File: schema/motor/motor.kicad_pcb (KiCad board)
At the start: 2 copper layers, 50 x 50 mm, 13 parts, among them IC1 RP2040_ZERO, J1 Conn_01x06, J2 Conn_02x04_Odd_Even, J4 Conn_01x04_Pin

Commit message: building motor pcb
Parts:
- added C10: 100n, Capacitor_SMD:C_0603_1608Metric, F.Cu at (123.8, 88.3)
- added C13: 10n, Capacitor_SMD:C_0603_1608Metric, F.Cu at (124.5, 78.7)
- added C6: 100n, Capacitor_SMD:C_0603_1608Metric, F.Cu at (123.8, 91.4)
- added C7: 10n, Capacitor_SMD:C_0603_1608Metric, F.Cu at (124.5, 85.1)
- added C8: 10n, Capacitor_SMD:C_0603_1608Metric, F.Cu at (124.5, 81.9)
- added R13: 1M0, Resistor_SMD:R_0603_1608Metric, F.Cu at (128.3, 85.1)
- added R14: 1M0, Resistor_SMD:R_0603_1608Metric, F.Cu at (128.3, 81.9)
- added R15: 100k, Resistor_SMD:R_0603_1608Metric, F.Cu at (126.4, 85.1)
- added R16: 100k, Resistor_SMD:R_0603_1608Metric, F.Cu at (126.4, 81.9)
- added R17: 100R, Resistor_SMD:R_0603_1608Metric, F.Cu at (131.4, 85.1)
- added R18: 100R, Resistor_SMD:R_0603_1608Metric, F.Cu at (135.3, 85.1)
- added R19: 100R, Resistor_SMD:R_0603_1608Metric, F.Cu at (133.3, 85.1)
- added R20: 100R, Resistor_SMD:R_0603_1608Metric, F.Cu at (137.2, 85.1)
- added R21: 100k, Resistor_SMD:R_0603_1608Metric, F.Cu at (126.4, 78.7)
- added R22: 1M0, Resistor_SMD:R_0603_1608Metric, F.Cu at (128.3, 78.7)
- moved C12 83.8 mm to (97.8, 70.5), turned to 180 degrees
- moved C9 83.5 mm to (97.8, 72.4), turned to 180 degrees
- moved R12 80.9 mm to (100.3, 86.4)
- moved R11 80.9 mm to (100.3, 83.8)
- moved C5 65.5 mm to (116.2, 66.0)
- moved J4 65.3 mm to (97.8, 82.5), turned to -90 degrees
- moved C4 25.6 mm to (100.3, 80.0), turned to -90 degrees
- moved C11 9.17 mm to (98.4, 74.9), turned to 180 degrees
- moved D3 0.40 mm to (98.4, 67.9)
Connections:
- IC1 pad 10: unconnected-(IC1-Pad10) -> BUTTON_R
- IC1 pad 12: unconnected-(IC1-Pad12) -> PWM_L
- IC1 pad 13: LED -> PWM_R
- IC1 pad 14: BUTTON_L -> ENABLE_L
- IC1 pad 15: BUTTON_R -> ENABLE_R
- IC1 pad 5: PWM_L -> unconnected-(IC1-Pad5)
- IC1 pad 6: PWM_R -> unconnected-(IC1-Pad6)
- IC1 pad 7: ENABLE_L -> unconnected-(IC1-Pad7)
- IC1 pad 8: ENABLE_R -> unconnected-(IC1-Pad8)
- IC1 pad 9: unconnected-(IC1-Pad9) -> BUTTON_L
- J2 pad 1: unconnected-(J2-Pin_1-Pad1) -> Net-(J2-Pin_1)
- J2 pad 2: unconnected-(J2-Pin_2-Pad2) -> Net-(J2-Pin_2)
- J2 pad 3: unconnected-(J2-Pin_3-Pad3) -> Net-(J2-Pin_3)
- J2 pad 4: unconnected-(J2-Pin_4-Pad4) -> Net-(J2-Pin_4)
- J2 pad 5: unconnected-(J2-Pin_5-Pad5) -> Net-(J2-Pin_5)
- J2 pad 6: unconnected-(J2-Pin_6-Pad6) -> Net-(J2-Pin_6)
- J2 pad 7: unconnected-(J2-Pin_7-Pad7) -> +3V3
- J2 pad 8: unconnected-(J2-Pin_8-Pad8) -> GND
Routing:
- net PWM_L: track 0.00 -> 31.9 mm
- net PWM_R: track 0.00 -> 26.1 mm
- net ENABLE_L: track 0.00 -> 19.5 mm
- net ENABLE_R: track 0.00 -> 17.3 mm
- net Net-(J2-Pin_6): track 0.00 -> 10.2 mm
- net SENSE_VIN: track 0.00 -> 7.52 mm
- net Net-(J2-Pin_2): track 0.00 -> 7.24 mm
- net Net-(J2-Pin_4): track 0.00 -> 6.72 mm
- net SENSE_R: track 0.00 -> 6.43 mm
- net Net-(J2-Pin_1): track 0.00 -> 3.91 mm
- net Net-(J2-Pin_5): track 0.00 -> 3.51 mm
- net Net-(J2-Pin_3): track 0.00 -> 3.39 mm
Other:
- outline, holes or cut-outs redrawn

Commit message: motor driver layout nearly done
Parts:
- added D2: BAV99, Package_TO_SOT_SMD:SOT-23, F.Cu at (133.0, 79.6)
- added D4: BAV99, Package_TO_SOT_SMD:SOT-23, F.Cu at (137.3, 79.5)
- added D5: BAV99, Package_TO_SOT_SMD:SOT-23, F.Cu at (141.6, 79.5)
- added H1: MountingHole, MountingHole:MountingHole_3.2mm_M3, F.Cu at (100.0, 90.0)
- added H2: MountingHole, MountingHole:MountingHole_3.2mm_M3, F.Cu at (140.0, 90.0)
- added H3: MountingHole, MountingHole:MountingHole_3.2mm_M3, F.Cu at (140.0, 50.0)
- added H4: MountingHole, MountingHole:MountingHole_3.2mm_M3, F.Cu at (100.0, 50.0)
- added Q1: DMG4800LK3-13, Package_TO_SOT_SMD:TO-252-3_TabPin2, F.Cu at (139.1, 71.6)
- added R10: 1k0, Resistor_SMD:R_0603_1608Metric, F.Cu at (138.7, 76.8)
- added R2: 10k, Resistor_SMD:R_0603_1608Metric, F.Cu at (131.6, 71.8)
- added R23: 1k0, Resistor_SMD:R_0603_1608Metric, F.Cu at (143.0, 76.8)
- added R3: 100R, Resistor_SMD:R_0603_1608Metric, F.Cu at (129.5, 71.8)
- added R4: 100R, Resistor_SMD:R_0603_1608Metric, F.Cu at (131.6, 76.8)
- added R5: 100R, Resistor_SMD:R_0603_1608Metric, F.Cu at (135.9, 76.8)
- added R6: 100R, Resistor_SMD:R_0603_1608Metric, F.Cu at (140.2, 76.8)
- added R9: 1k0, Resistor_SMD:R_0603_1608Metric, F.Cu at (134.4, 76.8)
- IC2: value ~ -> +5V reg
- moved R22 27.1 mm to (103.1, 68.6), turned to 180 degrees
- moved C5 13.1 mm to (103.1, 67.1), turned to 180 degrees
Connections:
- IC1 pad 11: unconnected-(IC1-Pad11) -> BUTTON
- IC1 pad 8: unconnected-(IC1-Pad8) -> LIGHT_ON
- J1 pad 1: unconnected-(J1-Pin_1-Pad1) -> Net-(J1-Pin_1)
- J1 pad 2: unconnected-(J1-Pin_2-Pad2) -> Net-(J1-Pin_2)
- J1 pad 3: unconnected-(J1-Pin_3-Pad3) -> Net-(J1-Pin_3)
- J1 pad 4: unconnected-(J1-Pin_4-Pad4) -> Net-(J1-Pin_4)
- J1 pad 5: unconnected-(J1-Pin_5-Pad5) -> GND
- J1 pad 6: unconnected-(J1-Pin_6-Pad6) -> VCC
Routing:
- net +5V: track 0.00 -> 56.8 mm, vias 0 -> 2
- net BUTTON_L: track 0.00 -> 38.5 mm, vias 0 -> 2
- net BUTTON_R: track 0.00 -> 38.4 mm, vias 0 -> 2
- net LIGHT_ON: track 0.00 -> 29.0 mm
- net BUTTON: track 0.00 -> 25.7 mm
- net Net-(J1-Pin_1): track 0.00 -> 25.0 mm, vias 0 -> 1
- net Net-(J1-Pin_4): track 0.00 -> 24.7 mm, vias 0 -> 2
- net Net-(D3-A): track 0.00 -> 23.0 mm
- net Net-(J1-Pin_3): track 0.00 -> 22.7 mm, vias 0 -> 1
- net SENSE_VIN: track 7.52 -> 29.4 mm, vias 0 -> 2
- net Net-(J1-Pin_2): track 0.00 -> 21.0 mm, vias 0 -> 1
- net VCC: track 0.00 -> 18.6 mm
- net GND: track 0.00 -> 13.1 mm, vias 0 -> 3
- net UART_TX: track 0.00 -> 9.49 mm, vias 0 -> 2
- net +3.3V: track 0.00 -> 9.16 mm
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- added copper zone on B.Cu, net GND
- added copper zone on F.Cu, net GND

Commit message: pravdepodobne starsi verze
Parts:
- removed D2, D4, D5: BAV99, Package_TO_SOT_SMD:SOT-23
- removed H1, H2, H3, H4: MountingHole, MountingHole:MountingHole_3.2mm_M3
- removed R10, R23, R9: 1k0, Resistor_SMD:R_0603_1608Metric
- removed R4, R5, R6: 100R, Resistor_SMD:R_0603_1608Metric
- added R8: 4k7, Resistor_SMD:R_0603_1608Metric, F.Cu at (157.0, 92.9)
- IC2: value +5V reg -> ~
- moved R22 27.1 mm to (128.3, 78.7), turned to 90 degrees
- moved C5 13.1 mm to (116.2, 66.0), turned to 0 degrees
- moved R2 12.8 mm to (142.2, 78.7), turned to 0 degrees
- moved R3 11.7 mm to (138.9, 78.7), turned to 0 degrees
- moved Q1 1.49 mm to (140.5, 71.0), turned to 90 degrees
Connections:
- IC1 pad 11: BUTTON -> LIGHT_ON
- IC1 pad 8: LIGHT_ON -> unconnected-(IC1-Pad8)
- J1 pad 2: Net-(J1-Pin_2) -> unconnected-(J1-Pin_2-Pad2)
- J1 pad 3: Net-(J1-Pin_3) -> unconnected-(J1-Pin_3-Pad3)
- J1 pad 4: Net-(J1-Pin_4) -> unconnected-(J1-Pin_4-Pad4)
- Q1 pad 2: Net-(J1-Pin_4) -> Net-(J1-Pin_1)
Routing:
- net +5V: track 56.8 -> 0.00 mm, vias 2 -> 0
- net BUTTON_L: track 38.5 -> 0.00 mm, vias 2 -> 0
- net BUTTON_R: track 38.4 -> 0.00 mm, vias 2 -> 0
- net LIGHT_ON: track 29.0 -> 0.00 mm
- net BUTTON: track 25.7 -> 0.00 mm
- net Net-(J1-Pin_1): track 25.0 -> 0.00 mm, vias 1 -> 0
- net Net-(J1-Pin_4): track 24.7 -> 0.00 mm, vias 2 -> 0
- net Net-(D3-A): track 23.0 -> 0.00 mm
- net Net-(J1-Pin_3): track 22.7 -> 0.00 mm, vias 1 -> 0
- net SENSE_VIN: track 29.4 -> 7.52 mm, vias 2 -> 0
- net Net-(J1-Pin_2): track 21.0 -> 0.00 mm, vias 1 -> 0
- net VCC: track 18.6 -> 0.00 mm
- net GND: track 13.1 -> 0.00 mm, vias 3 -> 0
- net UART_TX: track 9.49 -> 0.00 mm, vias 2 -> 0
- net +3.3V: track 9.16 -> 0.00 mm
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- removed copper zone on B.Cu, net GND
- removed copper zone on F.Cu, net GND

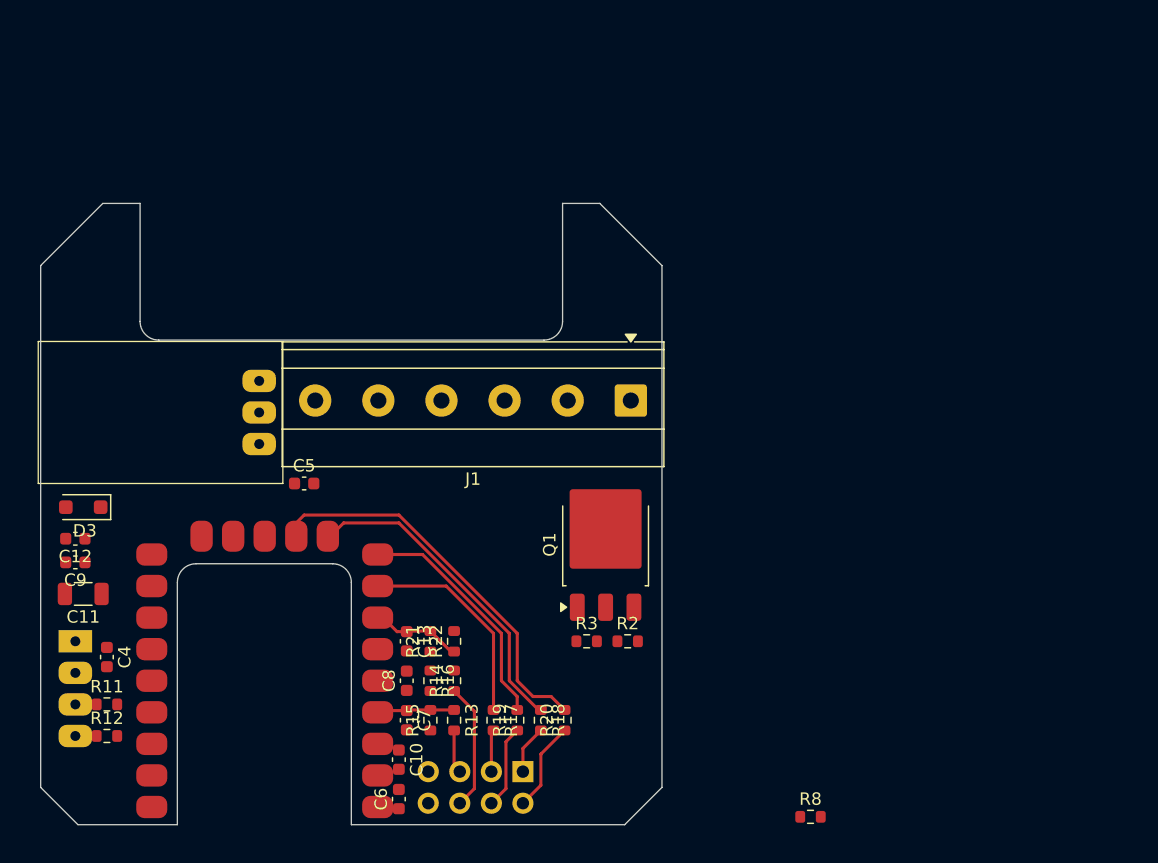
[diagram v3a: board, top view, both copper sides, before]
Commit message: layout done, silk screen needed
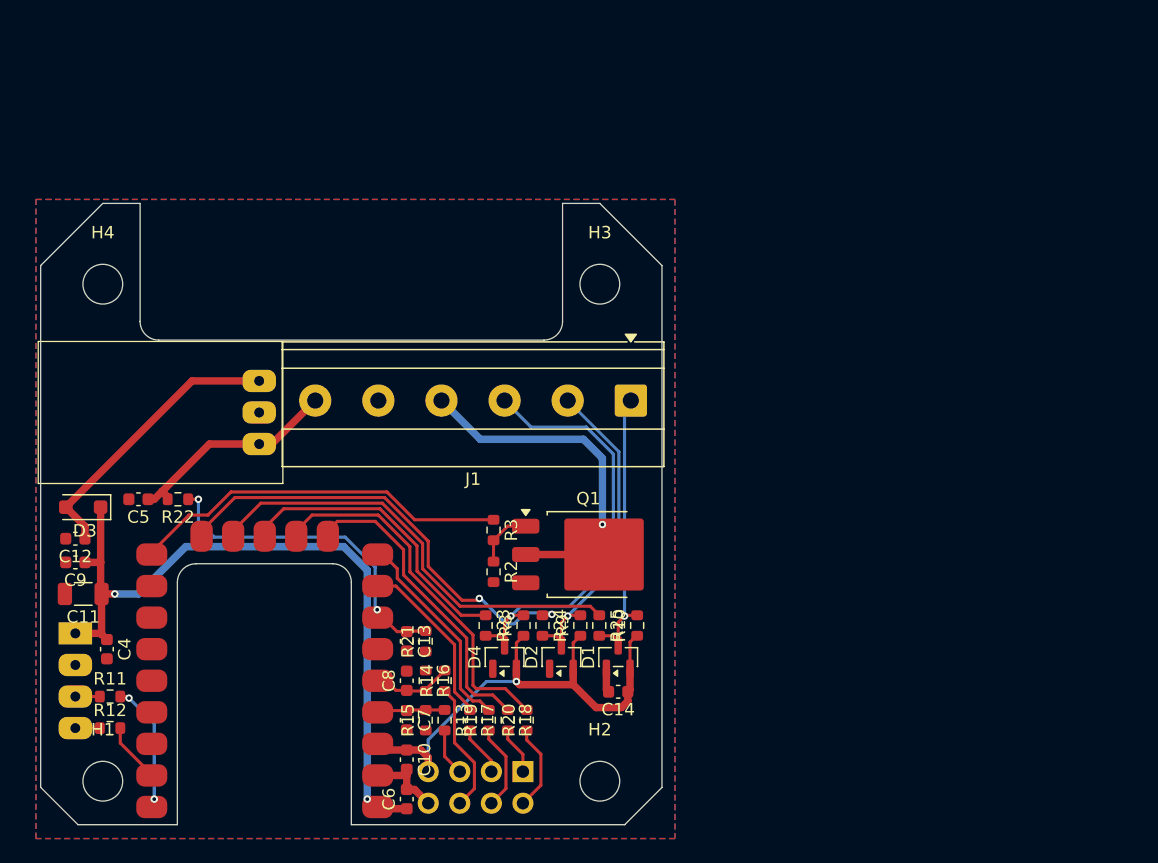
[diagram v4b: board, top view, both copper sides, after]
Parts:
- added C14: 100n, Capacitor_SMD:C_0603_1608Metric, F.Cu at (141.5, 82.8)
- added D1: BAV99, Package_TO_SOT_SMD:SOT-23, F.Cu at (141.5, 80.0)
- added D2: BAV99, Package_TO_SOT_SMD:SOT-23, F.Cu at (136.9, 80.0)
- added D4: BAV99, Package_TO_SOT_SMD:SOT-23, F.Cu at (132.3, 80.0)
- added H1: MountingHole, MountingHole:MountingHole_3.2mm_M3, F.Cu at (100.0, 90.0)
- added H2: MountingHole, MountingHole:MountingHole_3.2mm_M3, F.Cu at (140.0, 90.0)
- added H3: MountingHole, MountingHole:MountingHole_3.2mm_M3, F.Cu at (140.0, 50.0)
- added H4: MountingHole, MountingHole:MountingHole_3.2mm_M3, F.Cu at (100.0, 50.0)
- added R10: 1k0, Resistor_SMD:R_0603_1608Metric, F.Cu at (143.0, 77.5)
- added R23: 100R, Resistor_SMD:R_0603_1608Metric, F.Cu at (130.8, 77.5)
- added R24: 100R, Resistor_SMD:R_0603_1608Metric, F.Cu at (135.4, 77.5)
- added R25: 100R, Resistor_SMD:R_0603_1608Metric, F.Cu at (140.0, 77.5)
- added R9: 1k0, Resistor_SMD:R_0603_1608Metric, F.Cu at (138.4, 77.5)
- R8: value 4k7 -> 1k0
- moved R8 27.8 mm to (133.9, 77.5), turned to 90 degrees
- moved R22 25.0 mm to (106.0, 67.3), turned to 180 degrees
- moved C5 13.4 mm to (102.9, 67.3), turned to 180 degrees
- moved R2 12.2 mm to (131.4, 73.2), turned to -90 degrees
- moved R3 11.7 mm to (131.4, 69.8), turned to -90 degrees
- moved R20 3.05 mm to (134.1, 85.1)
- moved R18 2.67 mm to (132.6, 85.1)
- moved R19 2.29 mm to (131.1, 85.1)
- moved R17 1.91 mm to (129.5, 85.1)
- moved Q1 1.60 mm to (139.1, 71.8), turned to 0 degrees
- moved R13 0.76 mm to (127.5, 85.1)
- moved R14 0.76 mm to (127.5, 81.9)
- moved R12 0.68 mm to (100.6, 85.7)
- moved R11 0.68 mm to (100.6, 83.2)
- moved C4 0.64 mm to (100.3, 79.4)
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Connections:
- IC1 pad 11: LIGHT_ON -> BUTTON
- IC1 pad 8: unconnected-(IC1-Pad8) -> LIGHT_ON
- J1 pad 2: unconnected-(J1-Pin_2-Pad2) -> Net-(J1-Pin_2)
- J1 pad 3: unconnected-(J1-Pin_3-Pad3) -> Net-(J1-Pin_3)
- J1 pad 4: unconnected-(J1-Pin_4-Pad4) -> Net-(J1-Pin_4)
- Q1 pad 2: Net-(J1-Pin_1) -> Net-(J1-Pin_4)
- R8 pad 2: BUTTON -> Net-(J1-Pin_3)
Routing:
- net +5V: track 0.00 -> 59.9 mm, vias 0 -> 2
- net +3V3: track 0.00 -> 43.9 mm, vias 0 -> 1
- net BUTTON_L: track 0.00 -> 36.7 mm, vias 0 -> 2
- net BUTTON_R: track 0.00 -> 35.9 mm
- net Net-(J1-Pin_3): track 0.00 -> 34.9 mm, vias 0 -> 1
- net LIGHT_ON: track 0.00 -> 30.5 mm
- net Net-(J1-Pin_4): track 0.00 -> 29.7 mm, vias 0 -> 1
- net Net-(J1-Pin_2): track 0.00 -> 26.4 mm, vias 0 -> 1
- net BUTTON: track 0.00 -> 24.0 mm
- net Net-(J1-Pin_1): track 0.00 -> 23.2 mm, vias 0 -> 1
- net Net-(D3-A): track 0.00 -> 22.9 mm
- net SENSE_VIN: track 7.52 -> 27.1 mm, vias 0 -> 2
- net VCC: track 0.00 -> 17.6 mm
- net UART_TX: track 0.00 -> 9.72 mm, vias 0 -> 2
- net GND: track 0.00 -> 8.28 mm
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- added copper zone on B.Cu, net GND
- added copper zone on F.Cu, net GND

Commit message: silkscreen (partof)
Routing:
- net GND: track 8.28 -> 11.0 mm, vias 0 -> 27

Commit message: silkscreen almost done
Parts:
- IC2: value ~ -> +5V REG
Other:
- board text added: "+24V -"
- board text added: "+5V"
- board text added: "-"
- board text added: "BTN1"
- board text added: "BTN2"
- board text added: "BTNL"
- board text added: "LIGHT"
- board text added: "RX"
- board text added: "TX"

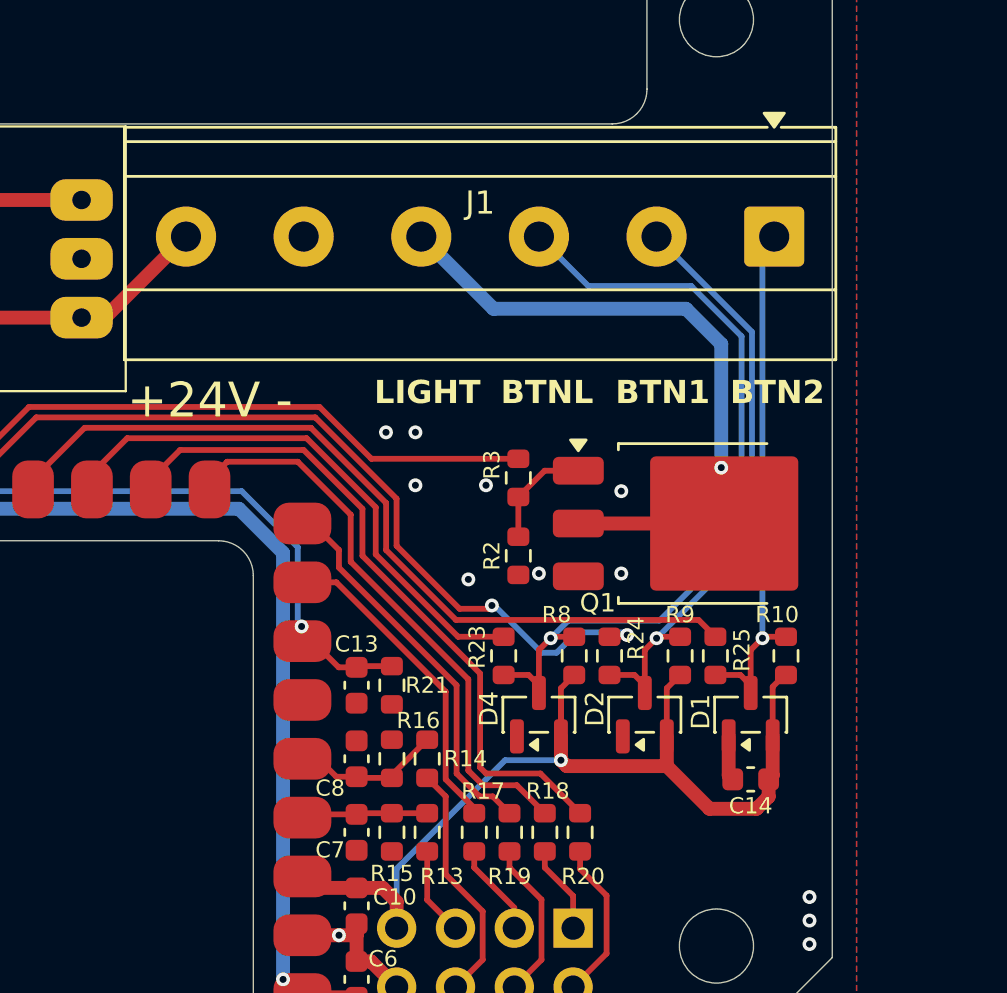
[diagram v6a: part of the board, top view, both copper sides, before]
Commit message: chicken picture missing, only
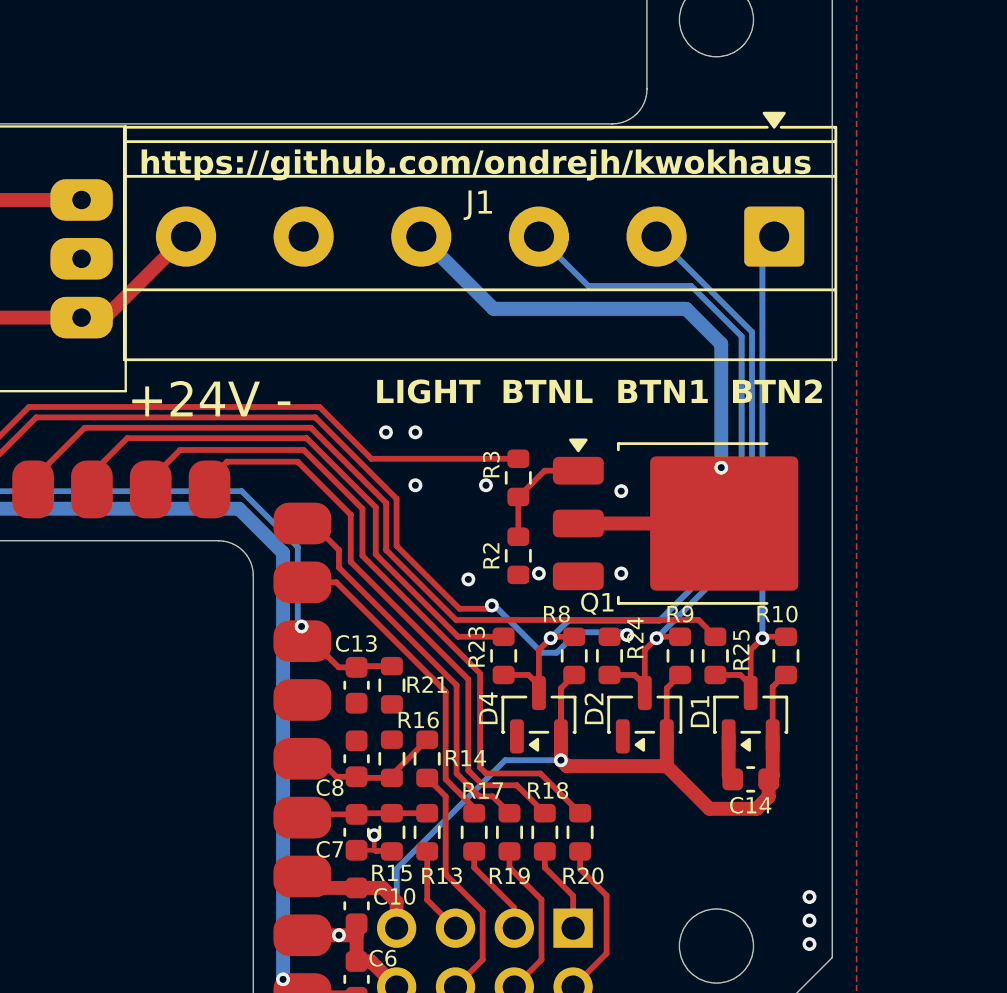
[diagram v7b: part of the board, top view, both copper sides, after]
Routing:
- net GND: track 11.0 -> 14.0 mm, vias 27 -> 28
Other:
- board text added: "Chicken Squasher v0.1"
- board text added: "OH2605"
- board text added: "https://github.com/ondrejh/kwokhaus"
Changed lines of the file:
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@@
 		(layer "Edge.Cuts")
+	)
+	(gr_text "https://github.com/ondrejh/kwokhaus"
+		(at 96.266 75.692 270)
+		(layer "B.Mask")
+		(effects
+			(font
+				(size 0.9 0.9)
+				(thickness 0.225)
+				(bold yes)
+			)
+			(justify left bottom mirror)
+		)
+	)
+	(gr_text "Chicken Squasher v0.1"
+		(at 98.425 67.945 270)
+		(layer "B.Mask")
+		(effects
+			(font
+				(size 0.9 0.9)
+				(thickness 0.225)
+				(bold yes)
+			)
+			(justify left bottom mirror)
+		)
+	)
+	(gr_text "OH2605"
+		(at 144.018 49.149 90)
+		(layer "B.Mask")
+		(effects
+			(font
+				(size 1.2 1.2)
+				(thickness 0.3)
+				(bold yes)
+			)
+			(justify left bottom mirror)
+		)
 	)
 	(gr_text "RX"
@@
 		)
 	)
+	(gr_text "https://github.com/ondrejh/kwokhaus"
+		(at 115.062 56.769 0)
+		(layer "F.SilkS")
+		(effects
+			(font
+				(size 1 1)
+				(thickness 0.25)
+				(bold yes)
+			)
+			(justify left bottom)
+		)
+	)
 	(gr_text "+24V -"
 		(at 114.554 67.31 0)
@@
 	)
 	(segment
+		(start 125.222 85.217)
+		(end 125.222 85.852)
+		(width 0.2)
+		(layer "F.Cu")
+		(net "GND")
+	)
+	(segment
+		(start 99.835 80.645)
+		(end 100.33 80.15)
+		(width 0.6)
+		(layer "F.Cu")
+		(net "GND")
+	)
+	(segment
 		(start 97.79 80.645)
 		(end 99.835 80.645)
@@
 	)
 	(segment
+		(start 124.46 85.865)
+		(end 125.934 85.865)
+		(width 0.2)
+		(layer "F.Cu")
+		(net "GND")
+	)
+	(segment
 		(start 140.528 80.9475)
 		(end 140.528 82.629)
@@
 	)
 	(segment
-		(start 99.835 80.645)
-		(end 100.33 80.15)
-		(width 0.6)
-		(layer "F.Cu")
-		(net "GND")
-	)
-	(segment
 		(start 124.46 89.535)
 		(end 124.46 89.04)
@@
 	)
 	(segment
+		(start 125.285 85.915)
+		(end 125.984 85.915)
+		(width 0.2)
+		(layer "F.Cu")
+		(net "GND")
+	)
+	(segment
 		(start 124.46 90.665)
 		(end 124.46 89.535)
@@
 		(net "GND")
 	)
+	(segment
+		(start 125.934 85.865)
+		(end 125.984 85.915)
+		(width 0.2)
+		(layer "F.Cu")
+		(net "GND")
+	)
+	(segment
+		(start 125.222 85.852)
+		(end 125.285 85.915)
+		(width 0.2)
+		(layer "F.Cu")
+		(net "GND")
+	)
 	(via
 		(at 139.192 44.704)
@@
 		(size 0.6)
 		(drill 0.3)
+		(layers "F.Cu" "B.Cu")
+		(free yes)
+		(net "GND")
+	)
+	(via
+		(at 125.222 85.217)
+		(size 0.6)
+		(drill 0.3)
